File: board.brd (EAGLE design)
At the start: 80 x 100 mm, 130 parts, among them IC1 LMZ10501SILT, IC2 TPS61088RHLR, Q1 IRFML8244TRPBF, Q2 IRFML8244TRPBF, Q3 IRFML8244TRPBF, Q4 IRFML8244TRPBF, Q5 IRFML8244TRPBF, U1 TB6612FNG, U3 STM32F405RG, U4 BMI088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

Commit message: switch layout on board
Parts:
- removed JP2: (no value), CASE-Pinhead:2X04
- removed S3: KMR621NGLFS, CASE-Switches:KMR621NGLFS
- added BTN_RST: KMR621NGLFS, CASE-Switches:KMR621NGLFS
- added DEBUG: (no value), CASE-Pinhead:2X04
- R32, R35, R36, R37: value 10k -> 0
- moved HC-05 386.6 mm to (49.6, 71.6)
- moved OLED 362.6 mm to (26.2, 67.3)
- moved C36 314.8 mm to (48.3, 7.52), turned to 180 degrees
- moved R31 239.4 mm to (30.1, 15.3), turned to 90 degrees
- moved C42 239.0 mm to (-31.6, -48.6)
- moved R28 237.8 mm to (30.1, 18.3), turned to 90 degrees
- moved R27 229.7 mm to (27.4, 15.2), turned to 90 degrees
- moved R26 228.1 mm to (27.4, 18.2), turned to 90 degrees
- moved R25 223.8 mm to (47.5, 11.5), turned to 90 degrees
- moved 5V_PWR 222.2 mm to (47.5, 14.4), turned to 180 degrees
- moved R24 207.0 mm to (42.6, 5.78), turned to 90 degrees
- moved R22 201.9 mm to (40.2, 5.79), turned to 90 degrees
- moved C35 189.1 mm to (45.5, 22.0), turned to 270 degrees
- moved C34 188.3 mm to (47.6, 22.0), turned to 270 degrees
- moved C32 165.0 mm to (48.8, 17.0)
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- renumbered S2 to BTN_SEL
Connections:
- removed net N$26: C33.2, R25.1, R_FBB.1
- net 3.3V: now also DEBUG.1, DEBUG.2; no longer JP2.1, JP2.2
- net GND: now also C33.2, DEBUG.3, DEBUG.4, R25.1, R_FBB.1; no longer JP2.3, JP2.4
- net N$30: now also BTN_RST.1, BTN_RST.2; no longer S3.1, S3.2
- net N$38: now also SW.1; no longer SW.3
- net RESET: now also BTN_RST.3, BTN_RST.4; no longer S3.3, S3.4
- net RX: now also DEBUG.5; no longer JP2.5
- net SWCLK: now also DEBUG.6; no longer JP2.6
- net SWDIO: now also DEBUG.8; no longer JP2.8
- net TX: now also DEBUG.7; no longer JP2.7
- net V_BAT: now also SW.3; no longer SW.1
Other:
- board text added: "RX"
- board text added: "SB01"
- board text added: "SB02"
- board text added: "SB03"
- board text added: "SB04"
- board text added: "TX"

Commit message: Eagle 9.5 persistent group update
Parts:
- removed D1, D2, D3, D7: SFH_4545, Isaks Bibliotek:SFH_4545
- removed IC1: LMZ10501SILT, Isaks Bibliotek:SON65P260X300X150-9N
- added FL_EMITTER, FR_EMITTER, L_EMITTER, R_EMITTER: SFH_4545, Isaks Bibliotek:SFH_4545
- added IC3: LMZ10501, Isaks Bibliotek:SON65P260X300X150-9N
- moved C7 139.8 mm to (27.8, 91.8), turned to 90 degrees
- moved C4 137.2 mm to (77.0, 7.34)
- moved C6 134.5 mm to (25.6, 91.9), turned to 90 degrees
- moved C5 134.4 mm to (73.8, 7.39)
- moved R16 134.0 mm to (66.9, 80.5), turned to 180 degrees
- moved C26 127.8 mm to (29.5, 18.0), turned to 270 degrees
- moved R1 123.6 mm to (13.7, 76.6), turned to 180 degrees
- moved C27 121.8 mm to (23.4, 13.4)
- moved U1 103.9 mm to (59.5, 64.4)
- moved C42 102.4 mm to (57.5, 1.83)
- moved C1 99.3 mm to (61.3, 57.4), turned to 180 degrees
- moved R34 95.3 mm to (21.8, 56.0)
- moved R33 94.5 mm to (21.5, 58.5)
- moved R8 92.7 mm to (10.1, 76.4), turned to 90 degrees
- moved C2 90.1 mm to (57.1, 57.4), turned to 0 degrees
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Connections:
- removed net N$28: U3.2, U3.3, U3.30, U3.4, U3.5, U3.6
- removed net N$29: U3.37, U3.38, U3.39, U3.45, U3.53
- removed net N$30: BTN_RST.1, BTN_RST.2, C36.2
- net 2V: now also FL_EMITTER.+, FR_EMITTER.+, IC3.3, IC3.5, L_EMITTER.+, R_EMITTER.+; no longer D1.+, D2.+, D3.+, D7.+, IC1.3, IC1.5
- net 5V: now also IC3.7; no longer IC1.7
- net GND: now also BTN_RST.1, BTN_RST.2, C36.2, IC3.4, IC3.6, IC3.9; no longer IC1.4, IC1.6, IC1.9
- net HEADER_RX: now also DEBUG.5
- net HEADER_TX: now also DEBUG.7
- net N$10: now also IC3.8; no longer IC1.8
- net N$11: now also IC3.2; no longer IC1.2
- net N$12: now also R_EMITTER.-; no longer D7.-
- net N$14: now also FR_EMITTER.-; no longer D3.-
- net N$2: now also L_EMITTER.-; no longer D1.-
- net N$5: now also FL_EMITTER.-; no longer D2.-
- net RX: no longer DEBUG.5
- net TX: no longer DEBUG.7
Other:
- board size 80 x 100 mm -> 80 x 110 mm
- board text added: "B"
- board text added: "Created by: Isak Åslund 2019-09"
- board text added: "G"
- board text added: "JERRY"
- board text added: "R"

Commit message: 3D Packages update
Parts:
- moved IC3 165.6 mm to (24.5, 86.5), turned to 180 degrees
- moved U4 62.9 mm to (52.3, 89.6), turned to 90 degrees
- moved FP1 60.0 mm to (52.3, 85.9), turned to 180 degrees
- moved C35 59.9 mm to (48.8, 90.8), turned to 90 degrees
- moved U$1 57.6 mm to (77.0, 7.23), turned to 0 degrees
- moved C34 57.6 mm to (46.7, 90.8), turned to 90 degrees
- moved C28 57.2 mm to (48.8, 87.6), turned to 270 degrees
- moved C29 54.8 mm to (46.7, 87.7), turned to 270 degrees
- moved C27 23.7 mm to (41.2, 29.1), turned to 180 degrees
- moved R12 18.0 mm to (62.1, 87.4)
- moved VR1 17.7 mm to (40.5, 24.5), turned to 0 degrees
- moved X1 16.2 mm to (25.1, 17.1)
- moved Q5 13.4 mm to (60.7, 84.6), turned to 0 degrees
- moved C13 13.1 mm to (55.6, 87.0), turned to 270 degrees
- moved C3 12.2 mm to (60.4, 66.2), turned to 180 degrees
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- renumbered JP1 to BOOT_JUMPERS

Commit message: More 3D Models
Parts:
- 5V_PWR, LED_B, LED_G, LED_R: value (none) -> CHIP-LED0603
- moved BOOT_JUMPERS 42.7 mm to (49.3, 96.8)

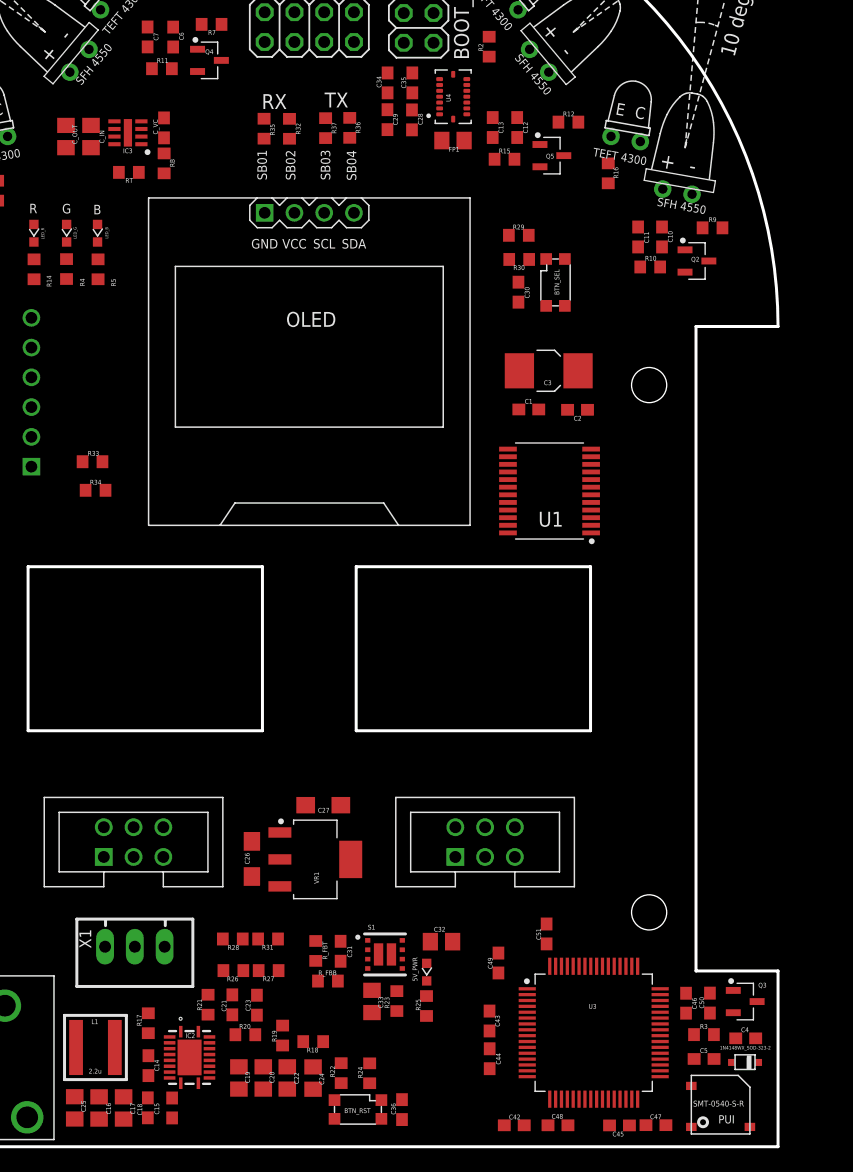
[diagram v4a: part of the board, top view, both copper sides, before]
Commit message: 3D packages and footprint updates + board picture
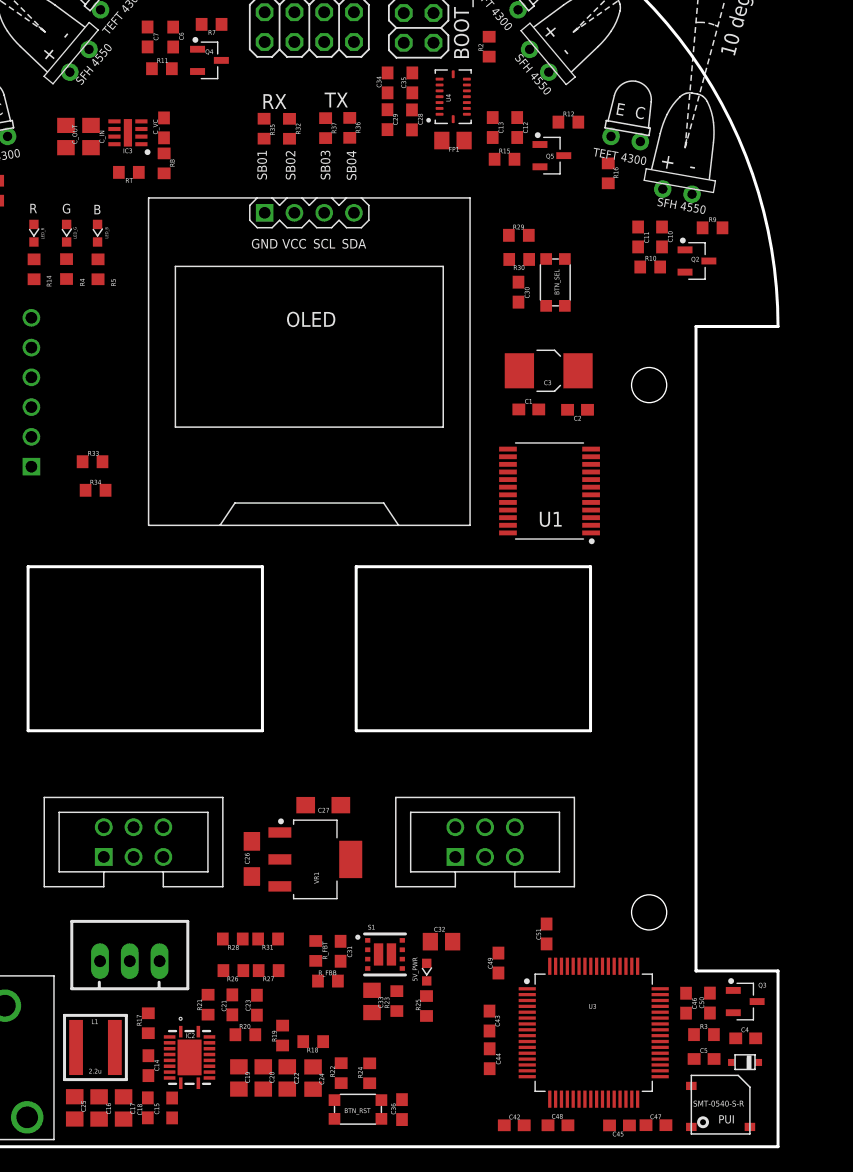
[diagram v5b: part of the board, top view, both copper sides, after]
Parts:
- removed X1: JST-XH, JST XH Connectors:JST-XH-03-PACKAGE-LONG-PAD
- added U$10: JST-XH-3, Isaks Bibliotek:JST-XH-03
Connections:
- net GND: now also U$10.1; no longer X1.1
- net N$33: now also U$10.2; no longer X1.2
- net N$38: now also U$10.3; no longer X1.3

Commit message: 3D packages + component layout
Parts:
- removed BOOT_JUMPERS: (no value), CASE-Pinhead:2X03
- added BOOT: (no value), CASE-Pinhead:2X03
- moved R3 84.0 mm to (17.3, 71.8)
- moved C5 84.0 mm to (17.3, 69.7)
- moved Q3 84.0 mm to (20.9, 74.6)
- moved U$4 84.0 mm to (18.6, 65.8)
- moved C4 84.0 mm to (20.9, 71.5)
- moved U$1 84.0 mm to (20.6, 69.5)
- moved BTN_RST 77.2 mm to (12.6, 73.7), turned to 90 degrees
- moved C36 75.6 mm to (12.7, 70.0), turned to 0 degrees
- moved C3 56.3 mm to (29.1, 19.4), turned to 90 degrees
- moved C1 53.8 mm to (38.1, 13.2), turned to 180 degrees
- moved C2 53.6 mm to (32.0, 19.0), turned to 90 degrees
- moved C26 47.1 mm to (77.8, 4.61), turned to 270 degrees
- moved U1 43.3 mm to (37.6, 19.2), turned to 270 degrees
- moved VR1 37.7 mm to (72.5, 4.50), turned to 180 degrees
- moved C27 35.7 mm to (66.6, 4.00), turned to 270 degrees
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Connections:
- net 3.3V: now also BOOT.1, BOOT.2; no longer BOOT_JUMPERS.1, BOOT_JUMPERS.2
- net GND: now also BOOT.5, BOOT.6; no longer BOOT_JUMPERS.5, BOOT_JUMPERS.6
- net N$32: now also BOOT.4; no longer BOOT_JUMPERS.4
- net N$34: now also BOOT.3; no longer BOOT_JUMPERS.3
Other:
- board size 80 x 110 mm -> 80 x 100 mm
- board text added: "0"
- board text added: "1"
- board text added: "3.3V"
- board text added: "BOOT0"
- board text added: "BOOT1"
- board text added: "GND"
- board text added: "RESET"
- board text added: "SWCLK"
- board text added: "SWDIO"
- board text removed: "Created by: Isak Åslund 2019-09"

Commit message: Routing power
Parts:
- added FP2: 10u, CASE-RCL:R0805
- added TP_12V, TP_2V, TP_3.3V, TP_5V: TEST-POINT3X5, Isaks Bibliotek:PAD.03X.05
- MOTOR_LEFT, MOTOR_RIGHT: value IDC-6PIN -> IE2-1024-ENCODER
- moved FP1 62.2 mm to (64.7, 6.46)
- moved U$6 28.4 mm to (28.8, 21.2)
- moved U$7 10.00 mm to (9.94, 5.87)
- moved R28 9.78 mm to (22.7, 16.4), turned to 90 degrees
- moved R31 8.10 mm to (22.7, 12.7), turned to 90 degrees
- moved R26 7.51 mm to (20.6, 16.4), turned to 90 degrees
- moved R27 5.16 mm to (20.6, 12.7), turned to 90 degrees
- moved C3 3.58 mm to (32.5, 18.6)
- moved C2 3.58 mm to (35.5, 18.2)
- moved U1 3.58 mm to (41.1, 18.4)
- moved C1 3.05 mm to (41.1, 12.7)
- moved C51 3.01 mm to (47.6, 8.47)
- moved C50 2.45 mm to (50.3, 21.4)
- moved C46 2.45 mm to (52.4, 21.4)
- moved C43 2.39 mm to (57.2, 5.55)
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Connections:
- net 12V: now also TP_12V.P$1
- net 2V: now also TP_2V.P$1
- net 3.3V: now also TP_3.3V.P$1
- net 5V: now also TP_5V.P$1
- net GND: now also FP2.1
- net GND_A: now also FP2.2
- net V_BAT: now also S1.7
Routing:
- net GND: track 0.00 -> 302.6 mm, vias 0 -> 6
- net L_RECEIVER: track 0.00 -> 145.1 mm, vias 0 -> 3
- net R_RECEIVER: track 0.00 -> 122.8 mm, vias 0 -> 1
- net RESET: track 0.00 -> 114.2 mm, vias 0 -> 2
- net BOOT0: track 0.00 -> 103.1 mm, vias 0 -> 2
- net FL_RECEIVER: track 0.00 -> 101.6 mm, vias 0 -> 2
- net 3.3VA: track 0.00 -> 99.6 mm, vias 0 -> 6
- net V_BAT: track 0.00 -> 97.6 mm, vias 0 -> 2
- net GND_A: track 0.00 -> 94.9 mm, vias 0 -> 2
- net 3.3V: track 0.00 -> 87.3 mm, vias 0 -> 6
- net FR_RECEIVER: track 0.00 -> 78.9 mm, vias 0 -> 2
- net 5V: track 0.00 -> 76.0 mm, vias 0 -> 5
- net VOLTM_CELL1: track 0.00 -> 53.7 mm, vias 0 -> 2
- net VOLTM_BATT: track 0.00 -> 48.9 mm, vias 0 -> 2
- net ENC_L_A: track 0.00 -> 40.0 mm, vias 0 -> 1
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- added copper zone on layer 1, net 12V
- added copper zone on layer 1, net 3.3V
- added copper zone on layer 1, net 5V
- added copper zone on layer 1, net GND
- added copper zone on layer 1, net GND_M
- added copper zone on layer 1, net GND_SW
- added copper zone on layer 1, net N$15
- added copper zone on layer 1, net V_BAT
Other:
- board text added: "Jerry V1.0 Designed by Isak Åslund Sweden | Fall 2019 github.com/elixir7/micromouse"

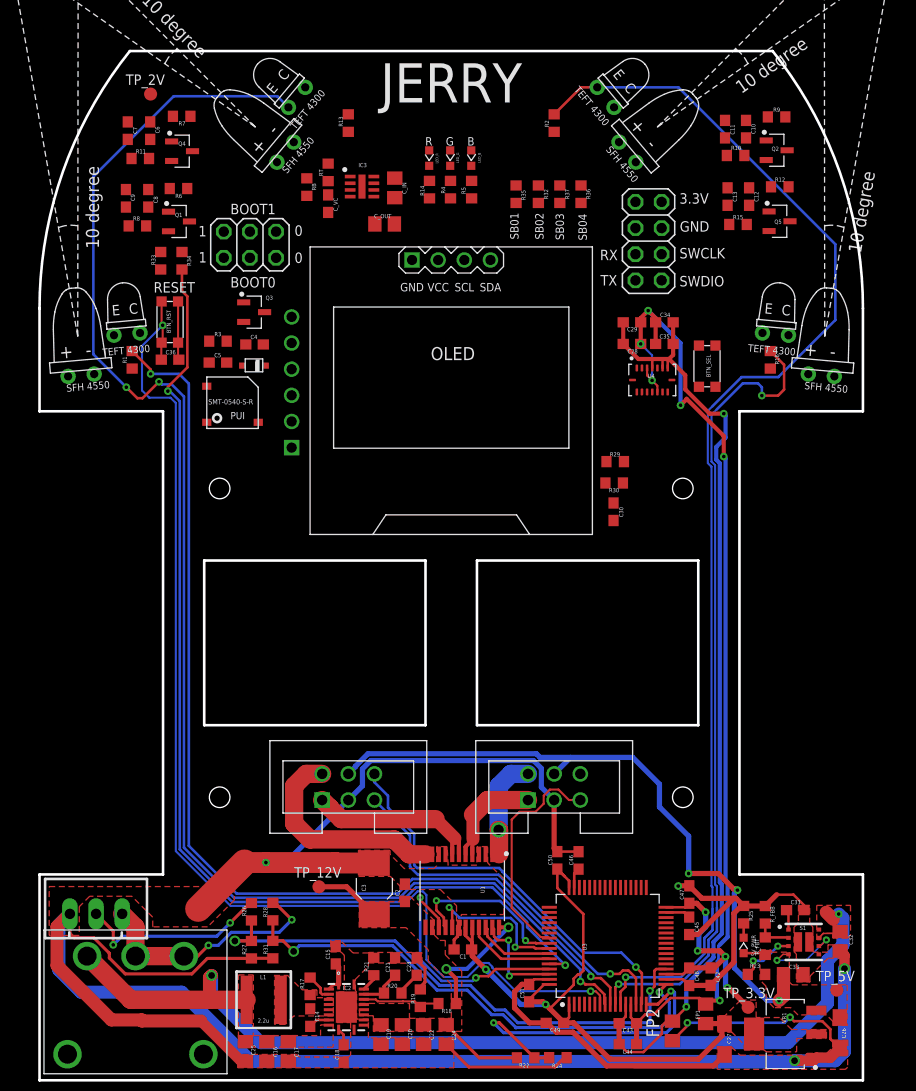
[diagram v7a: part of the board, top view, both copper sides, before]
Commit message: Routing top side
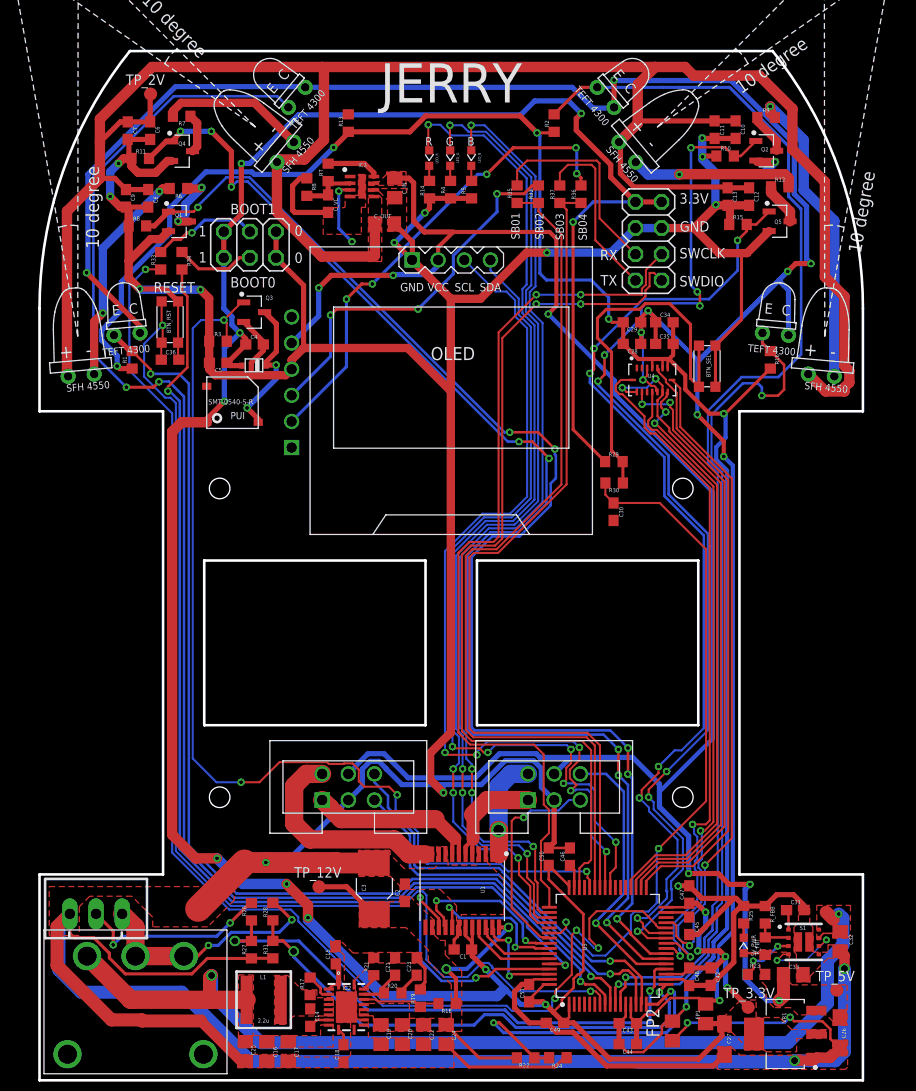
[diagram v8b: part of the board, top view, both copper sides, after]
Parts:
- moved C10 1.02 mm to (67.6, 92.4)
- moved Q2 1.02 mm to (70.6, 90.3)
- moved R9 1.02 mm to (70.6, 93.5)
- moved C11 1.02 mm to (65.6, 92.4)
- moved R10 1.02 mm to (66.6, 89.8)
- moved C46 0.91 mm to (51.5, 21.7)
- moved C50 0.91 mm to (49.5, 21.7)
- moved R29 0.13 mm to (55.8, 60.1)
- moved R35 0.10 mm to (46.4, 86.1), turned to 90 degrees
- turned C5 to 180 degrees
- turned R32 to 90 degrees
- turned R36 to 90 degrees
- turned R37 to 90 degrees
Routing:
- net GND: track 302.6 -> 559.8 mm, vias 6 -> 18
- net 2V: track 0.00 -> 218.2 mm, vias 0 -> 2
- net 3.3V: track 87.3 -> 286.4 mm, vias 6 -> 14
- net 3.3VA: track 99.6 -> 229.8 mm, vias 6 -> 10
- net L_EMITTER: track 0.00 -> 127.6 mm, vias 0 -> 8
- net BOOT1: track 0.00 -> 127.2 mm, vias 0 -> 4
- net FL_EMITTER: track 0.00 -> 124.4 mm, vias 0 -> 6
- net 5V: track 76.0 -> 185.1 mm, vias 5 -> 8
- net FR_EMITTER: track 0.00 -> 104.6 mm, vias 0 -> 8
- net BUZZER: track 0.00 -> 99.2 mm, vias 0 -> 4
- net LED_R: track 0.00 -> 98.8 mm, vias 0 -> 4
- net LED_G: track 0.00 -> 96.5 mm, vias 0 -> 4
- net R_EMITTER: track 0.00 -> 95.0 mm, vias 0 -> 6
- net LED_B: track 0.00 -> 94.6 mm, vias 0 -> 4
- net GND_A: track 94.9 -> 189.0 mm, vias 2 -> 6
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- added copper zone on layer 1, net 2V
